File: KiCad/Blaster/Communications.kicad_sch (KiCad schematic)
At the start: 0 parts

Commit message: Blaster Power and Communications schematic updates. Add Revision B schematic
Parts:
- added C12: 10nF, symbol Device:C
- added C13: 4.7µF, symbol Device:C
- added C14, C15: 0.1µF, symbol Device:C
- added C16, C17: 47pF, symbol Device:C
- added D5: TX, LED_SMD:LED_0805_2012Metric_Pad1.15x1.40mm_HandSolder, symbol Device:LED_Filled
- added D6: RX, LED_SMD:LED_0805_2012Metric_Pad1.15x1.40mm_HandSolder, symbol Device:LED_Filled
- added J7: USB_B_Micro, symbol Connector:USB_B_Micro
- added L2: 2.2µH, symbol Device:L
- added R23, R24: 3.3kΩ, symbol Device:R_US
- added R25: 10kΩ, symbol Device:R_US
- added TP32: RX, 0_AKeller_Footprints:1x1_100mil_Header, symbol 0_AKeller_Parts:Test_Point
- added TP33: TX, 0_AKeller_Footprints:1x1_100mil_Header, symbol 0_AKeller_Parts:Test_Point
- added TP34: D+, 0_AKeller_Footprints:1x1_100mil_Header, symbol 0_AKeller_Parts:Test_Point
- added TP35: D-, 0_AKeller_Footprints:1x1_100mil_Header, symbol 0_AKeller_Parts:Test_Point
- added U7: FT232RL, Package_SO:SSOP-28_5.3x10.2mm_P0.65mm, symbol Interface_USB:FT232RL
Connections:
- new net: R25.2, U7.14 (CBUS3)
- new net: C17.1, J7.3 (D+), TP34.1, U7.15 (USBD+)
- new net: C16.1, J7.2 (D-), TP35.1, U7.16 (USBD-)
- new net: C15.2, U7.17 (3V3OUT)
- new net: R24.2, U7.22 (CBUS1)
- new net: R23.2, U7.23 (CBUS0)
- new net: D6.1 (K), R24.1
- new net: D5.1 (K), R23.1
- new net: C12.1, J7.1 (VBUS), L2.1
- new net GND: C12.2, C13.2, C14.2, C15.1, C16.2, C17.2, J7.5 (GND), J7.6 (Shield), U7.18 (GND), U7.21 (GND), U7.25 (AGND), U7.26 (TEST), U7.7 (GND)
- new net RX: TP32.1, U7.1 (TXD)
- new net TX: TP33.1, U7.5 (RXD)
- new net VBUS: C13.1, C14.1, D5.2 (A), D6.2 (A), L2.2, R25.1, U7.20 (VCC)
- no-connect marks 0 -> 13

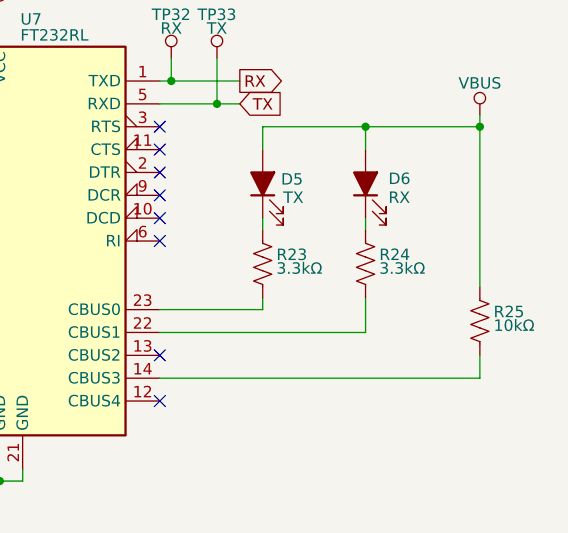
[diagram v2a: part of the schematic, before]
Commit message: Assign blaster footprints, Create Blaster PCB Outline
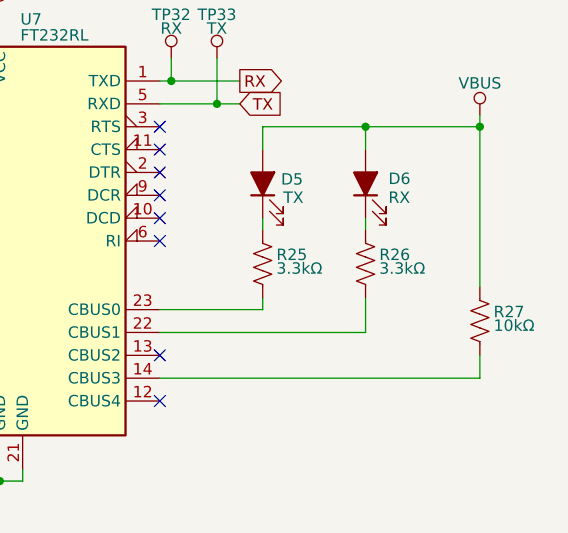
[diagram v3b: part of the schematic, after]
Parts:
- C12, C13, C14, C15, C16, C17: footprint (none) -> Capacitor_SMD:C_0805_2012Metric_Pad1.18x1.45mm_HandSolder
- J7: footprint (none) -> 0_AKeller_Footprints:USB_Micro-B_Amphenol
- L2: footprint (none) -> Inductor_SMD:L_0805_2012Metric_Pad1.15x1.40mm_HandSolder
- R25: renamed from R23; footprint (none) -> Resistor_SMD:R_0805_2012Metric_Pad1.20x1.40mm_HandSolder
- R26: renamed from R24; footprint (none) -> Resistor_SMD:R_0805_2012Metric_Pad1.20x1.40mm_HandSolder
- R27: renamed from R25; footprint (none) -> Resistor_SMD:R_0805_2012Metric_Pad1.20x1.40mm_HandSolder
- U7: footprint Package_SO:SSOP-28_5.3x10.2mm_P0.65mm -> 0_AKeller_Footprints:SSOP-28
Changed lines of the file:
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@@
 			)
 		)
-		(property "Footprint" "Package_SO:SSOP-28_5.3x10.2mm_P0.65mm"
+		(property "Footprint" "0_AKeller_Footprints:SSOP-28"
 			(at 161.29 121.92 0)
 			(effects
@@
 		(dnp no)
 		(fields_autoplaced yes)
-		(property "Reference" "#PWR052"
+		(property "Reference" "#PWR054"
 			(at 77.47 107.95 0)
 			(effects
@@
 			(project "Project"
 				(path "/152b0fc1-fa29-4f64-bd5c-6a59f63b05cf/f727b983-1be0-41f0-9150-1b1a8c10c4b2"
-					(reference "#PWR052")
+					(reference "#PWR054")
 					(unit 1)
 				)
@@
 		(dnp no)
 		(fields_autoplaced yes)
-		(property "Reference" "#PWR047"
+		(property "Reference" "#PWR049"
 			(at 106.68 77.47 0)
 			(effects
@@
 			(project "Project"
 				(path "/152b0fc1-fa29-4f64-bd5c-6a59f63b05cf/f727b983-1be0-41f0-9150-1b1a8c10c4b2"
-					(reference "#PWR047")
+					(reference "#PWR049")
 					(unit 1)
 				)
@@
 		(dnp no)
 		(fields_autoplaced yes)
-		(property "Reference" "#PWR054"
+		(property "Reference" "#PWR056"
 			(at 101.6 110.49 0)
 			(effects
@@
 			(project "Project"
 				(path "/152b0fc1-fa29-4f64-bd5c-6a59f63b05cf/f727b983-1be0-41f0-9150-1b1a8c10c4b2"
-					(reference "#PWR054")
+					(reference "#PWR056")
 					(unit 1)
 				)
@@
 		(dnp no)
 		(fields_autoplaced yes)
-		(property "Reference" "#PWR050"
+		(property "Reference" "#PWR052"
 			(at 102.87 88.9 0)
 			(effects
@@
 			(project "Project"
 				(path "/152b0fc1-fa29-4f64-bd5c-6a59f63b05cf/f727b983-1be0-41f0-9150-1b1a8c10c4b2"
-					(reference "#PWR050")
+					(reference "#PWR052")
 					(unit 1)
 				)
@@
 		(on_board yes)
 		(dnp no)
-		(property "Reference" "R24"
+		(property "Reference" "R26"
 			(at 178.054 100.584 0)
 			(effects
@@
 			)
 		)
-		(property "Footprint" ""
+		(property "Footprint" "Resistor_SMD:R_0805_2012Metric_Pad1.20x1.40mm_HandSolder"
 			(at 177.546 101.854 90)
 			(effects
@@
 			(project "Project"
 				(path "/152b0fc1-fa29-4f64-bd5c-6a59f63b05cf/f727b983-1be0-41f0-9150-1b1a8c10c4b2"
-					(reference "R24")
+					(reference "R26")
 					(unit 1)
 				)
@@
 		(dnp no)
 		(fields_autoplaced yes)
-		(property "Reference" "#PWR048"
+		(property "Reference" "#PWR050"
 			(at 118.11 77.47 0)
 			(effects
@@
 			(project "Project"
 				(path "/152b0fc1-fa29-4f64-bd5c-6a59f63b05cf/f727b983-1be0-41f0-9150-1b1a8c10c4b2"
-					(reference "#PWR048")
+					(reference "#PWR050")
 					(unit 1)
 				)
@@
 			)
 		)
-		(property "Footprint" ""
+		(property "Footprint" "Capacitor_SMD:C_0805_2012Metric_Pad1.18x1.45mm_HandSolder"
 			(at 107.6452 71.12 0)
 			(effects
@@
 		(on_board no)
 		(dnp no)
-		(property "Reference" "#PWR049"
+		(property "Reference" "#PWR051"
 			(at 135.636 73.66 0)
 			(effects
@@
 			(project "Project"
 				(path "/152b0fc1-fa29-4f64-bd5c-6a59f63b05cf/f727b983-1be0-41f0-9150-1b1a8c10c4b2"
-					(reference "#PWR049")
+					(reference "#PWR051")
 					(unit 1)
 				)
@@
 			)
 		)
-		(property "Footprint" ""
+		(property "Footprint" "Capacitor_SMD:C_0805_2012Metric_Pad1.18x1.45mm_HandSolder"
 			(at 94.9452 71.12 0)
 			(effects
@@
 		(on_board no)
 		(dnp no)
-		(property "Reference" "#PWR045"
+		(property "Reference" "#PWR047"
 			(at 117.856 59.69 0)
 			(effects
@@
 			(project ""
 				(path "/152b0fc1-fa29-4f64-bd5c-6a59f63b05cf/f727b983-1be0-41f0-9150-1b1a8c10c4b2"
-					(reference "#PWR045")
+					(reference "#PWR047")
 					(unit 1)
 				)
@@
 			)
 		)
-		(property "Footprint" ""
+		(property "Footprint" "Capacitor_SMD:C_0805_2012Metric_Pad1.18x1.45mm_HandSolder"
 			(at 102.5652 104.14 0)
 			(effects
@@
 			)
 		)
-		(property "Footprint" ""
+		(property "Footprint" "Capacitor_SMD:C_0805_2012Metric_Pad1.18x1.45mm_HandSolder"
 			(at 119.0752 71.12 0)
 			(effects
@@
 			)
 		)
-		(property "Footprint" ""
+		(property "Footprint" "Capacitor_SMD:C_0805_2012Metric_Pad1.18x1.45mm_HandSolder"
 			(at 92.4052 104.14 0)
 			(effects
@@
 		(dnp no)
 		(fields_autoplaced yes)
-		(property "Reference" "#PWR056"
+		(property "Reference" "#PWR058"
 			(at 130.81 133.35 0)
 			(effects
@@
 			(project "Project"
 				(path "/152b0fc1-fa29-4f64-bd5c-6a59f63b05cf/f727b983-1be0-41f0-9150-1b1a8c10c4b2"
-					(reference "#PWR056")
+					(reference "#PWR058")
 					(unit 1)
 				)
@@
 		(dnp no)
 		(fields_autoplaced yes)
-		(property "Reference" "#PWR055"
+		(property "Reference" "#PWR057"
 			(at 111.76 124.46 0)
 			(effects
@@
 			(project "Project"
 				(path "/152b0fc1-fa29-4f64-bd5c-6a59f63b05cf/f727b983-1be0-41f0-9150-1b1a8c10c4b2"
-					(reference "#PWR055")
+					(reference "#PWR057")
 					(unit 1)
 				)
@@
 		(on_board yes)
 		(dnp no)
-		(property "Reference" "R25"
+		(property "Reference" "R27"
 			(at 190.754 106.934 0)
 			(effects
@@
 			)
 		)
-		(property "Footprint" ""
+		(property "Footprint" "Resistor_SMD:R_0805_2012Metric_Pad1.20x1.40mm_HandSolder"
 			(at 190.246 108.204 90)
 			(effects
@@
 			(project "Project"
 				(path "/152b0fc1-fa29-4f64-bd5c-6a59f63b05cf/f727b983-1be0-41f0-9150-1b1a8c10c4b2"
-					(reference "R25")
+					(reference "R27")
 					(unit 1)
 				)
@@
 		(dnp no)
 		(fields_autoplaced yes)
-		(property "Reference" "#PWR053"
+		(property "Reference" "#PWR055"
 			(at 91.44 110.49 0)
 			(effects
@@
 			(project "Project"
 				(path "/152b0fc1-fa29-4f64-bd5c-6a59f63b05cf/f727b983-1be0-41f0-9150-1b1a8c10c4b2"
-					(reference "#PWR053")
+					(reference "#PWR055")
 					(unit 1)
 				)
@@
 			)
 		)
-		(property "Footprint" ""
+		(property "Footprint" "Capacitor_SMD:C_0805_2012Metric_Pad1.18x1.45mm_HandSolder"
 			(at 111.76 80.3148 0)
 			(effects
@@
 			)
 		)
-		(property "Footprint" ""
+		(property "Footprint" "Inductor_SMD:L_0805_2012Metric_Pad1.15x1.40mm_HandSolder"
 			(at 100.33 60.96 0)
 			(effects
@@
 		(on_board no)
 		(dnp no)
-		(property "Reference" "#PWR051"
+		(property "Reference" "#PWR053"
 			(at 188.976 85.09 0)
 			(effects
@@
 			(project "Project"
 				(path "/152b0fc1-fa29-4f64-bd5c-6a59f63b05cf/f727b983-1be0-41f0-9150-1b1a8c10c4b2"
-					(reference "#PWR051")
+					(reference "#PWR053")
 					(unit 1)
 				)
@@
 		(on_board yes)
 		(dnp no)
-		(property "Reference" "R23"
+		(property "Reference" "R25"
 			(at 166.624 100.584 0)
 			(effects
@@
 			)
 		)
-		(property "Footprint" ""
+		(property "Footprint" "Resistor_SMD:R_0805_2012Metric_Pad1.20x1.40mm_HandSolder"
 			(at 166.116 101.854 90)
 			(effects
@@
 			(project "Project"
 				(path "/152b0fc1-fa29-4f64-bd5c-6a59f63b05cf/f727b983-1be0-41f0-9150-1b1a8c10c4b2"
-					(reference "R23")
+					(reference "R25")
 					(unit 1)
 				)
@@
 			)
 		)
-		(property "Footprint" ""
+		(property "Footprint" "0_AKeller_Footprints:USB_Micro-B_Amphenol"
 			(at 82.55 90.17 0)
 			(effects
@@
 		(dnp no)
 		(fields_autoplaced yes)
-		(property "Reference" "#PWR046"
+		(property "Reference" "#PWR048"
 			(at 93.98 77.47 0)
 			(effects
@@
 			(project "Project"
 				(path "/152b0fc1-fa29-4f64-bd5c-6a59f63b05cf/f727b983-1be0-41f0-9150-1b1a8c10c4b2"
-					(reference "#PWR046")
-					(unit 1)
-				)
+					(reference "#PWR048")
+					(unit 1)
+				)

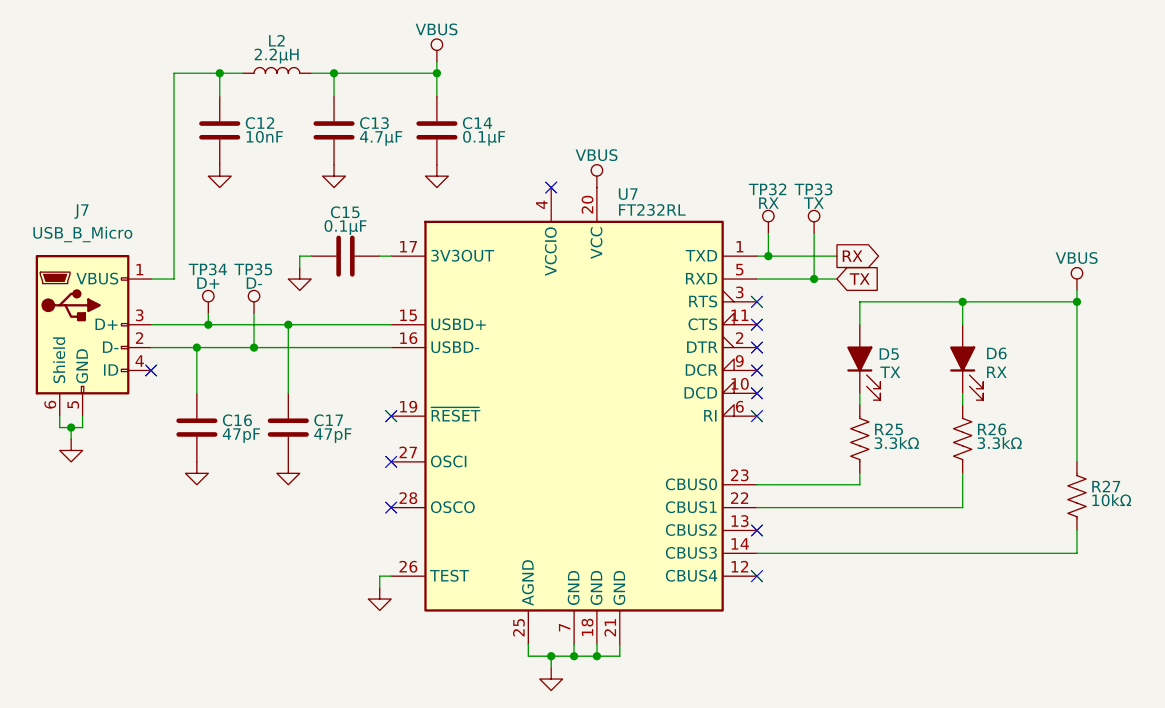
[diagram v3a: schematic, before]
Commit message: Complete Blaster PCB layout and traces
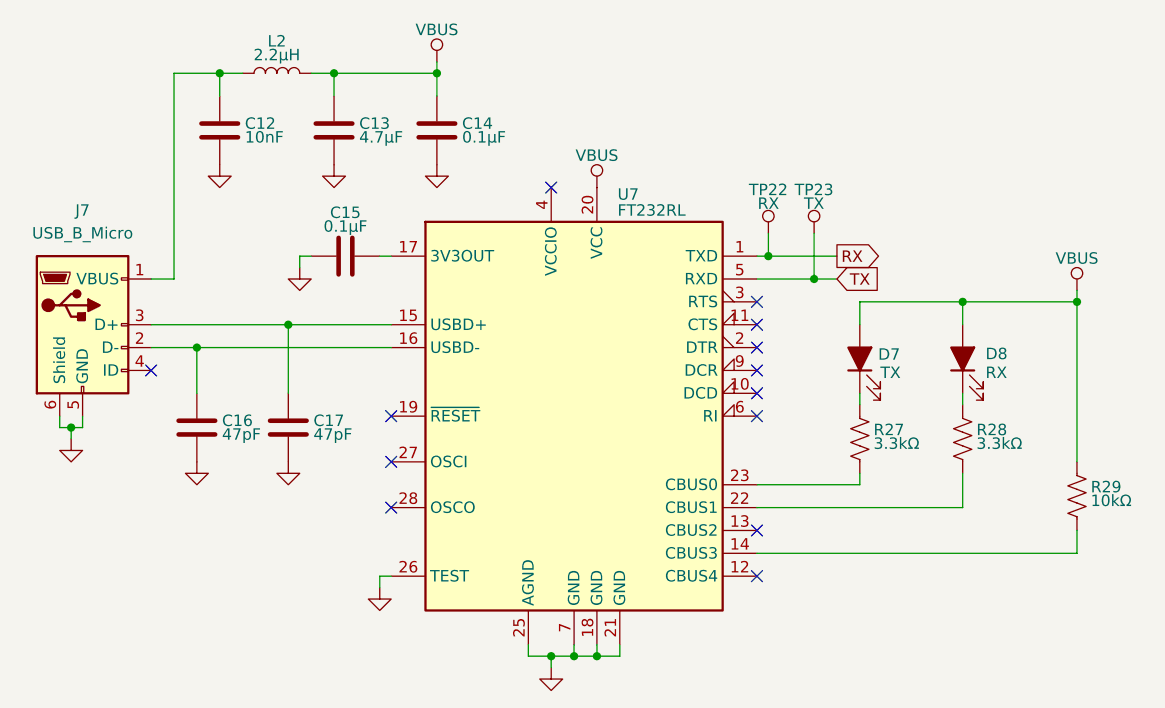
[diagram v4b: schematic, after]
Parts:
- removed TP34: D+, 0_AKeller_Footprints:1x1_100mil_Header, symbol 0_AKeller_Parts:Test_Point
- removed TP35: D-, 0_AKeller_Footprints:1x1_100mil_Header, symbol 0_AKeller_Parts:Test_Point
- renumbered D5 to D7, D6 to D8, R25 to R27, R26 to R28, R27 to R29, TP32 to TP22, TP33 to TP23
